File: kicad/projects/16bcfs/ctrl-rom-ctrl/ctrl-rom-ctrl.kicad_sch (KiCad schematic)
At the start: 88 parts, among them J1 Signal Header, J2 Power, J3 Power, J4 Control ROM Address, J5 Raw Address for Pgm ROM, J6 Instruction, U1 74HC74, U10 74HC193, U11 74HC193, U12 74HC193, U13 74HC193, U14 74HC165, U15 74HC541, U16 74HC541, U17 74HC541, U2 74HC00, U3 74HC08, U4 74HC03, U5 74HC157, U6 74HC157, U7 74HC157, U8 74HC157, U9 74HC193, X1 XO32, X2 XO32

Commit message: Add additional changes
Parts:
- removed unit 4 of U2
- removed X2: XO32, Oscillator:Oscillator_DIP-14, symbol Oscillator:XO32
- added C1, C2, C3, C4, C5: 0u1, symbol Device:C
- added D23: Green, symbol Device:LED
- added R23: 1K, symbol Device:R_US
- added U19: 74HC04, symbol 74xx:74HC04
- added U21, U22: 74HC08, symbol eryjus:74HC08
- added U23: 74HC32, symbol eryjus:74HC32
- added unit 4 of U6
- added unit 3 of U6
- added unit 2 of U7
- added unit 5 of U7
- added unit 1 of U7
- added unit 3 of U7
- J4: renamed from J1; symbol Connector:Conn_01x10_Pin -> Connector:Conn_01x16_Pin
- U1: renamed from U3; EmulatorName (none) -> and1
- U2: renamed from U1; EmulatorName (none) -> resetting
- U3: renamed from U4; EmulatorName (none) -> oNand1
- U6: renamed from U2; EmulatorName (none) -> nand1
- U7: renamed from U2; EmulatorName (none) -> nand2
- X1: footprint Oscillator:Oscillator_DIP-8 -> eryjus:Oscillator_DIP-8-14; symbol Oscillator:XO32 -> eryjus:XO32-Dual
- renumbered C5 to C10, C6 to C11, C7 to C12, C8 to C13, C9 to C14, C10 to C15, C11 to C16, C12 to C17, C13 to C18, C14 to C19, C15 to C20, C16 to C21, C17 to C22, C18 to C23, C19 to C24, C1 to C6, C2 to C7, C3 to C8, C4 to C9, D8 to D1, D17 to D10, D18 to D11, D19 to D12, D20 to D13, D21 to D14, D22 to D15, D4 to D16, D5 to D17, D6 to D18, D7 to D19, D9 to D2, D1 to D20, D2 to D21, D3 to D22, D10 to D3, D11 to D4, D12 to D5, D13 to D6, D14 to D7, D15 to D8, D16 to D9, J6 to J1, J4 to J2, J5 to J3, J2 to J5, J3 to J6, R8 to R1, R17 to R10, R18 to R11, R19 to R12, R20 to R13, R21 to R14, R22 to R15, R4 to R16, R5 to R17, R6 to R18, R7 to R19, R9 to R2, R1 to R20, R2 to R21, R3 to R22, R10 to R3, R11 to R4, R12 to R5, R13 to R6, R14 to R7, R15 to R8, R16 to R9, U17 to U10, U5 to U11, U6 to U12, U7 to U13, U8 to U14, U10 to U15, U11 to U16, U12 to U17, U13 to U18, U9 to U4, U15 to U5, U16 to U8, U14 to U9
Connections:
- net Bits Counter ~{BO}: now also U21.13; no longer U1.5, U15.5 (UP)
- net CPY_CLK: now also J4.15 (Pin_15), U22.3; no longer J4.7 (Pin_7), U1.3, U4.4 (DOWN)
- net GNDREF: now also J4.14 (Pin_14), J4.16 (Pin_16), X1.4 (GND), X1.7 (GND), C1.2, C2.2, C3.2, C4.2, C5.2, R23.2, U19.7 (GND), U21.7 (GND), U22.10, U22.12, U22.13, U22.7 (GND), U22.9, U23.7 (GND), U7.10, U7.7 (GND), U7.9; no longer J4.9 (Pin_9), U1.10, U1.12, U1.13, U1.9, U10.6 (A4), U4.14 (CLR), U4.15 (A), X1.2 (GND)
- net QC: now also J4.11 (Pin_11), U3.1, U3.2, U22.5
- net QR: now also U23.13; no longer U9.1 (~{PL})
- net RAW_CPY_CLK: now also U4.4 (DOWN), X1.11 (OUT), X1.8 (OUT), U19.1; no longer J4.10 (Pin_10), X1.3 (OUT)
- net VCC: now also U4.15 (A), X1.14 (V+), C1.1, C2.1, C3.1, C4.1, C5.1, U19.14 (VCC), U21.14 (VCC), U22.14 (VCC), U23.14 (VCC), U7.14 (VCC); no longer X1.4 (V+)
- net ~{QC}: now also U4.14 (CLR), U23.12
- net ~{QR}: now also U9.1 (~{PL}), U21.12, U22.2; no longer U1.4
- net at U1.8: now also U21.10, U21.5
- net at U10.14 (Y4): now also D23.2 (A)
- net at U1.11: now also U1.10
- net Bit0 renamed Ba
- net Ba: now also U1.9, U23.1
- net Bit1 renamed Bb
- net Bb: now also U19.3, U23.2
- net Bit2 renamed Bc
- net Bc: now also U19.5, U23.4
- net Bit3 renamed Bd
- net Bd: now also U19.9, U21.9, U23.5
- removed net Bits Load: U1.6, U3.1, U3.2, U4.11 (~{LOAD})
- net CMD_ADDR renamed EEPROM CMD/ADDR
- net EEPROM CMD/ADDR: now also J4.10 (Pin_10); no longer J4.8 (Pin_8)
- net RESET renamed ~{RESET}
- net ~{RESET}: now also U7.12, U7.13; no longer U7.10, U7.9
- net ~{Reset} renamed Reset
- net Reset: now also U7.11; no longer U7.8
- new net: U19.11, U21.8
- new net: U19.13, U21.6
- new net: U19.2, U21.1
- new net: U23.3, U23.9
- new net: U1.12, U19.6
- new net: U1.3, U1.4
- new net: U23.10, U23.6
- new net: U19.8, U21.2
- new net: U21.3, U21.4
- new net: U1.13, U19.4
- new net: U1.6, U22.1
- new net: D23.1 (K), R23.1
- new net 0-Bit Count: U23.8, U7.1
- new net EEPROM ~{CS}: J4.9 (Pin_9), U23.11
- new net QL: U7.3, U7.4
- new net QS: J4.7 (Pin_7), U1.5, U10.6 (A4), U15.5 (UP), U22.4, U6.10, U6.11
- new net SRAM ~{CE}: J4.13 (Pin_13), U22.6
- new net ~{1-Bit Count Low Clock}: U19.12, U6.9, U7.5
- new net ~{1-Bit Count}: U19.10, U6.13
- new net ~{QL}: J4.12 (Pin_12), U7.2, U7.6
- new net ~{QS}: J4.8 (Pin_8), U6.12, U6.8
- new net ~{Qr} * /BO: U21.11, U4.11 (~{LOAD})
- no-connect marks 15 -> 14
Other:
- note added: "Latching SR Latch"
- note added: "SRAM ~{CE}"
- note added: "SRAM ~{OE}"
- note added: "SRAM ~{WE}"
- note added: "Shifting SR Latch"
- moved on the sheet: C10, C11, C12, C13, C14, C15, C16, C17, C18, C19, C20, C21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

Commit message: Create and Integrate a Control ROM Module (#116)
* Fixes #108
* Closes #109
* Closes #110
* Closes #111
* Closes #114
* Closes #115
* Closes #107

Co-authored-by: Adam Clark <adam@eryjus.com>
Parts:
- added D24: Red, symbol Device:LED
- added R24: 1K, symbol Device:R_US
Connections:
- net GNDREF: now also R24.2; no longer U14.13 (I1d), U8.9 (A7)
- net RAW_CPY_CLK: no longer U2.3 (C)
- net at U8.11 (Y7): now also D24.2 (A)
- net ~{Raw_Cpy_Clk}: now reaches U19.2, U21.1
- net ~{Raw_Cpy_Clk}: now also U2.3 (C)
- net PGM_AF: now reaches U18.7 (QD)
- net PGM_AF: now also U14.13 (I1d)
- net ROM_AF: now reaches U14.12 (Zd)
- net ROM_AF: now also U8.9 (A7)
- new net: D24.1 (K), R24.1
- no-connect marks 14 -> 11

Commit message: Control ROM Control Cleanup (#133)
* Closes #123
* Closes #132
* Completes #119
* Defers #89
* Defers #122
* Defers #121
* Defers #120

Co-authored-by: Adam Clark <adam@eryjus.com>
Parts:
- removed D16, D17, D18, D19: Red, symbol Device:LED
- removed D20, D21, D23: Green, symbol Device:LED
- removed D22: Blue, symbol Device:LED
- removed R16, R17, R18, R19, R20, R21, R22, R23: 1K, symbol Device:R_US
- removed U10: 74HC541, symbol eryjus:74HC541
- added R25, R26: 0R, symbol Device:R_US
- X1: now not fitted
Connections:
- net GNDREF: now also J4.6 (Pin_6), J4.8 (Pin_8); no longer U2.11 (C), U2.12 (D)
- net QC: now also U2.12 (D); no longer J4.5 (Pin_5), U11.1 (S), U12.1 (S), U13.1 (S), U14.1 (S), U3.1, U3.2
- net QR: no longer J4.3 (Pin_3)
- net QS: no longer J4.7 (Pin_7)
- net RAW_CPY_CLK: now also R25.2, R26.1; no longer X1.11 (OUT), X1.8 (OUT)
- net VCC: no longer U2.13 (~{R})
- net ~{QC}: no longer J4.6 (Pin_6)
- net ~{QR}: now also J4.3 (Pin_3); no longer J4.4 (Pin_4)
- net ~{QS}: no longer J4.8 (Pin_8)
- net ~{RESET}: now also U2.13 (~{R})
- net ~{Raw_Cpy_Clk}: now also U2.11 (C)
- net DONE: now reaches U2.8 (~{Q})
- net DONE: now also J4.5 (Pin_5)
- net ~{DONE}: now reaches U2.9 (Q)
- net ~{DONE}: now also J4.4 (Pin_4), U11.1 (S), U12.1 (S), U13.1 (S), U14.1 (S), U3.1, U3.2
- new net: R25.1, X1.11 (OUT), X1.8 (OUT)
- new net RAW_SYS_CLK: J4.7 (Pin_7), R26.2
- no-connect marks 11 -> 9
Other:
- note added: "Done D-Type Latch"
- note added: "LATCH ENABLE"
- note added: "SHIFT ENABLE"
- note added: "SHIFT RESET"
- moved on the sheet: U2B, U3A, U7D

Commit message: Video 0099 (#147)
Control ROM Control Module PCB Design & Free-Running the Emulator

* Closes #140
* Closes #89
* Closes #141
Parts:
- removed C10: 0u1, symbol Device:C
- added C25: 47u, Capacitor_SMD:C_1206_3216Metric_Pad1.33x1.80mm_HandSolder, symbol Device:C
- added R16, R17, R18, R19, R20, R21, R22, R23, R27, R28, R29, R30, R31, R32, R33, R34, R35, R36: 0R, Resistor_SMD:R_1206_3216Metric_Pad1.30x1.75mm_HandSolder, symbol Device:R_US
- C1, C11, C12, C13, C14, C15, C16, C17, C18, C19, C2, C20, C21, C22, C24, C3, C4, C5, C6, C7, C8, C9: footprint (none) -> Capacitor_SMD:C_1206_3216Metric_Pad1.33x1.80mm_HandSolder
- C23: footprint (none) -> Capacitor_SMD:C_1206_3216Metric_Pad1.33x1.80mm_HandSolder; now not fitted
- D1, D10, D11, D12, D13, D14, D15, D2, D24, D3, D4, D5, D6, D7, D8, D9: footprint (none) -> LED_SMD:LED_1206_3216Metric_Pad1.42x1.75mm_HandSolder
- J1, J2, J3, J4: footprint (none) -> Connector_PinHeader_2.54mm:PinHeader_1x16_P2.54mm_Vertical
- J5, J6: footprint (none) -> Connector_PinHeader_2.54mm:PinHeader_1x02_P2.54mm_Vertical
- R1, R10, R11, R12, R13, R14, R15, R2, R24, R25, R26, R3, R4, R5, R6, R7, R8, R9: footprint (none) -> Resistor_SMD:R_1206_3216Metric_Pad1.30x1.75mm_HandSolder
- U1, U19, U2, U21, U22, U23, U3, U6, U7: footprint (none) -> Package_SO:SOIC-14_3.9x8.7mm_P1.27mm
- U11, U12, U13, U14, U15, U16, U17, U18, U4, U9: footprint (none) -> Package_SO:SOIC-16_3.9x9.9mm_P1.27mm
- U5, U8: footprint (none) -> Package_SO:SOIC-20W_7.5x12.8mm_P1.27mm
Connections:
- net GNDREF: now also C25.2, R16.1, R17.1, R18.1, R19.1, R22.1, R27.1, R28.1, R30.1, R31.1, R33.1, R34.1, R36.1; no longer U22.10, U22.12, U22.13, U22.9, U3.10, U3.12, U3.13, U3.4, U3.5, U3.9, U7.10, U7.9
- net VCC: now also C25.1
- net at U22.11: now also R29.1
- net at U22.8: now also R23.1
- net at U3.8: now also R32.1
- net at U3.6: now also R20.1
- net at U7.8: now also R21.1
- net at U3.11: now also R35.1
- new net: R22.2, U22.9
- new net: R34.2, U3.12
- new net: R33.2, U3.10
- new net: R17.2, U3.5
- new net: R16.2, U3.4
- new net: R28.2, U22.12
- new net: R30.2, U22.13
- new net: R27.2, U22.10
- new net: R18.2, U7.9
- new net: R36.2, U3.13
- new net: R31.2, U3.9
- new net: R19.2, U7.10
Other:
- moved on the sheet: C24, U22C, U22D, U3B, U3C, U3D, U7C

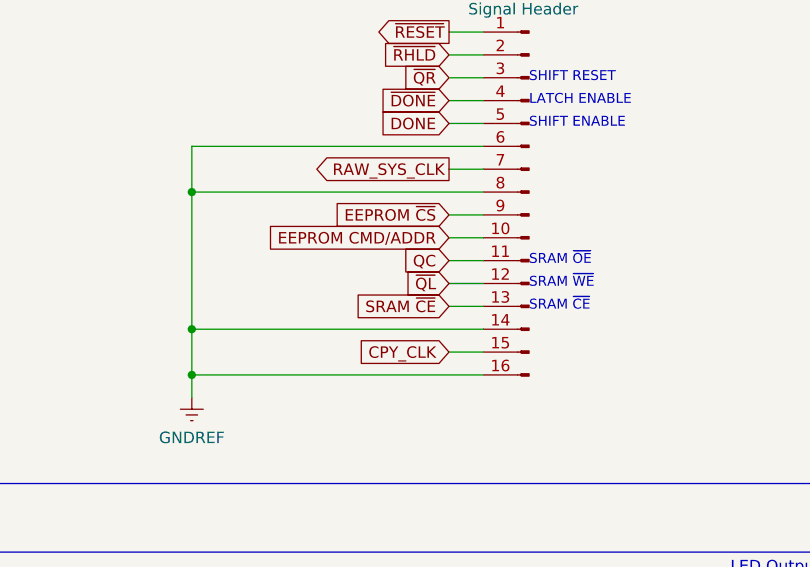
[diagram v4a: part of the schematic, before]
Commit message: Create the Reset Module and (mostly) debug it
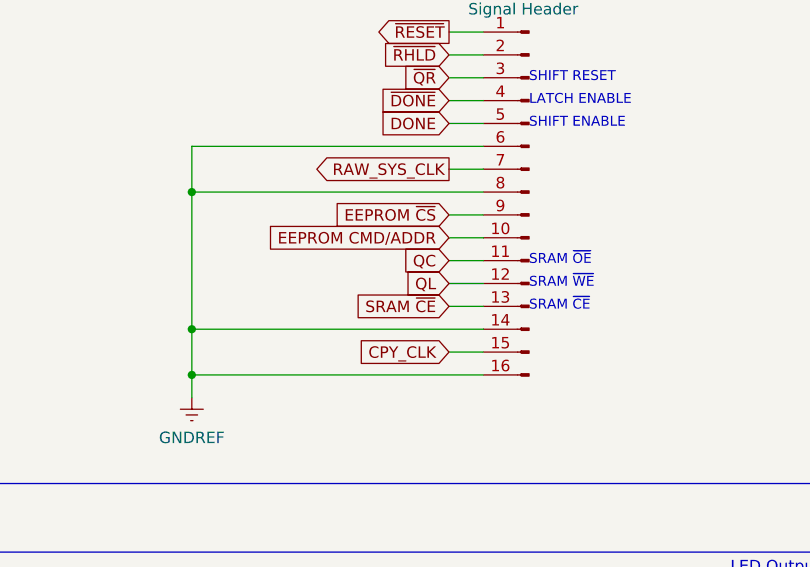
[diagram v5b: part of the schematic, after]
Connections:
- net QL: now also J4.12 (Pin_12)
- net ~{QL}: no longer J4.12 (Pin_12)
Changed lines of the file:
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@@
     )
   )
-  (global_label "~{QL}" (shape input) (at 495.3 161.29 180) (fields_autoplaced)
+  (global_label "QL" (shape input) (at 495.3 161.29 180) (fields_autoplaced)
     (effects (font (size 1.27 1.27)) (justify right))
     (property "Intersheetrefs" "${INTERSHEET_REFS}" (at 489.9562 161.29 0)

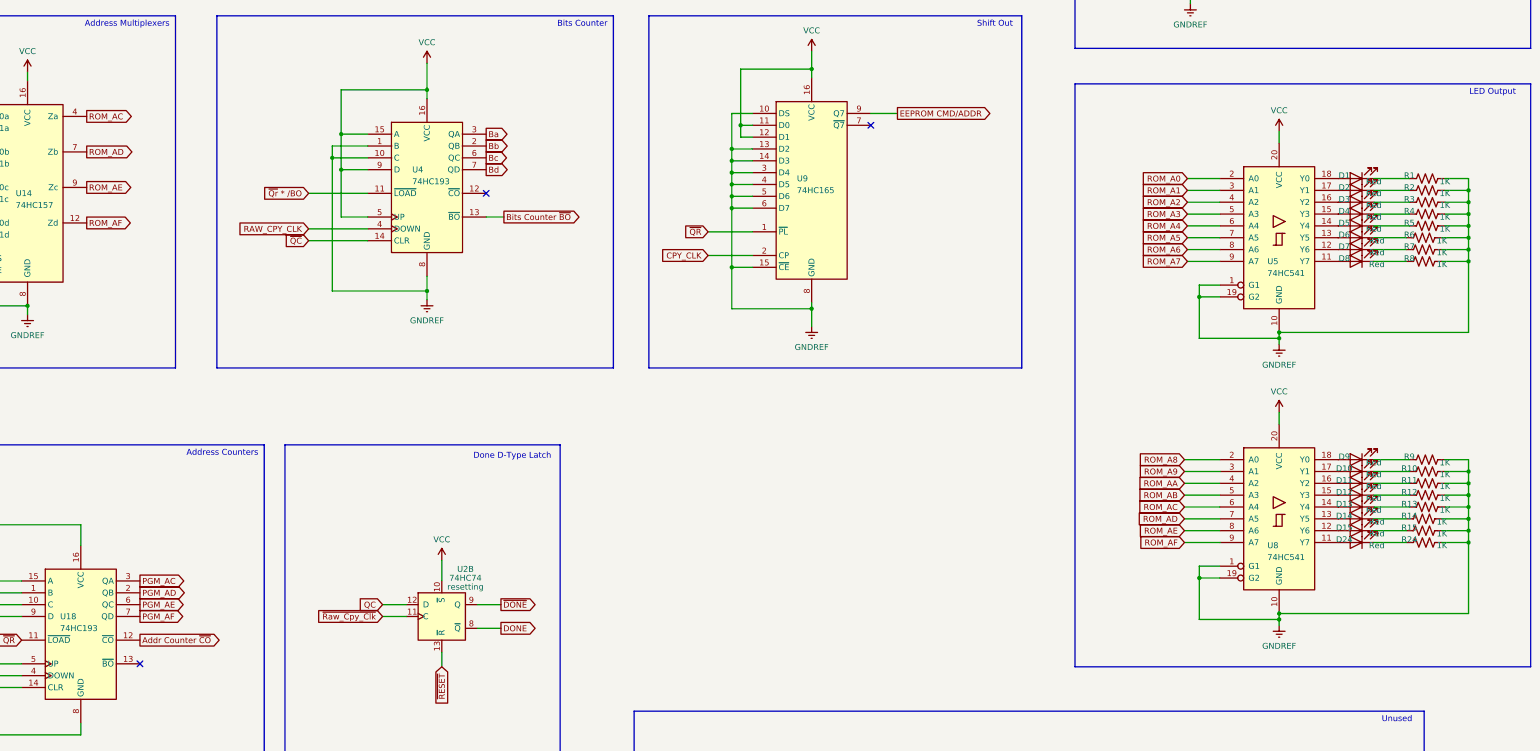
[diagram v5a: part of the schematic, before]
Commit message: Remove the LEDs from the Control ROM Control Module
The LEDs are not populated on the first iteration PCB.  Remove them from
the schematic and from the PCB design.
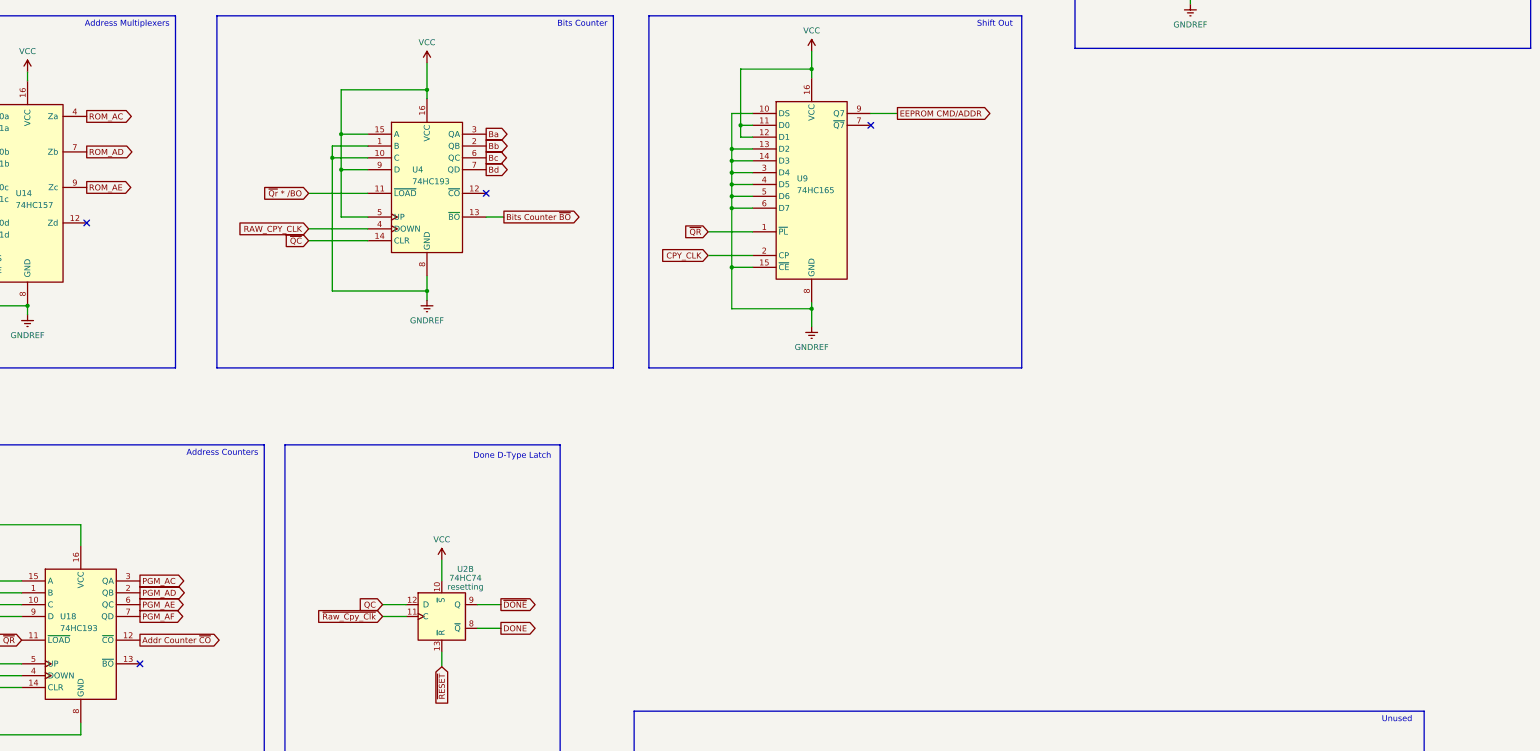
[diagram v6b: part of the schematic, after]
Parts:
- removed D1, D10, D11, D12, D13, D14, D15, D2, D24, D3, D4, D5, D6, D7, D8, D9: Red, LED_SMD:LED_1206_3216Metric_Pad1.42x1.75mm_HandSolder, symbol Device:LED
- removed R1, R10, R11, R12, R13, R14, R15, R2, R24, R3, R4, R5, R6, R7, R8, R9: 1K, Resistor_SMD:R_1206_3216Metric_Pad1.30x1.75mm_HandSolder, symbol Device:R_US
- removed U5, U8: 74HC541, Package_SO:SOIC-20W_7.5x12.8mm_P1.27mm, symbol eryjus:74HC541
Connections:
- net ROM_AF: no longer names the net of U14.12 (Zd)
- no-connect marks 9 -> 10
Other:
- note removed: "LED Output"
